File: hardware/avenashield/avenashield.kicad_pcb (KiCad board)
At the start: 4 copper layers, 115 x 78 mm, 128 parts, among them J1 Bus_PCI_Express_Mini, J10 Lattepanda Lower Left Header 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, J11 12V DC IN Headers, J12 EXT PWR IN, J13 LED_OUT, J14 JAE_MM60-EZH059-B5-R650, J2 SIM_Card, J3 CAN_TRA_HEADER, J4 CAN_IMP_HEADER, J5 USB Headers Board Top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

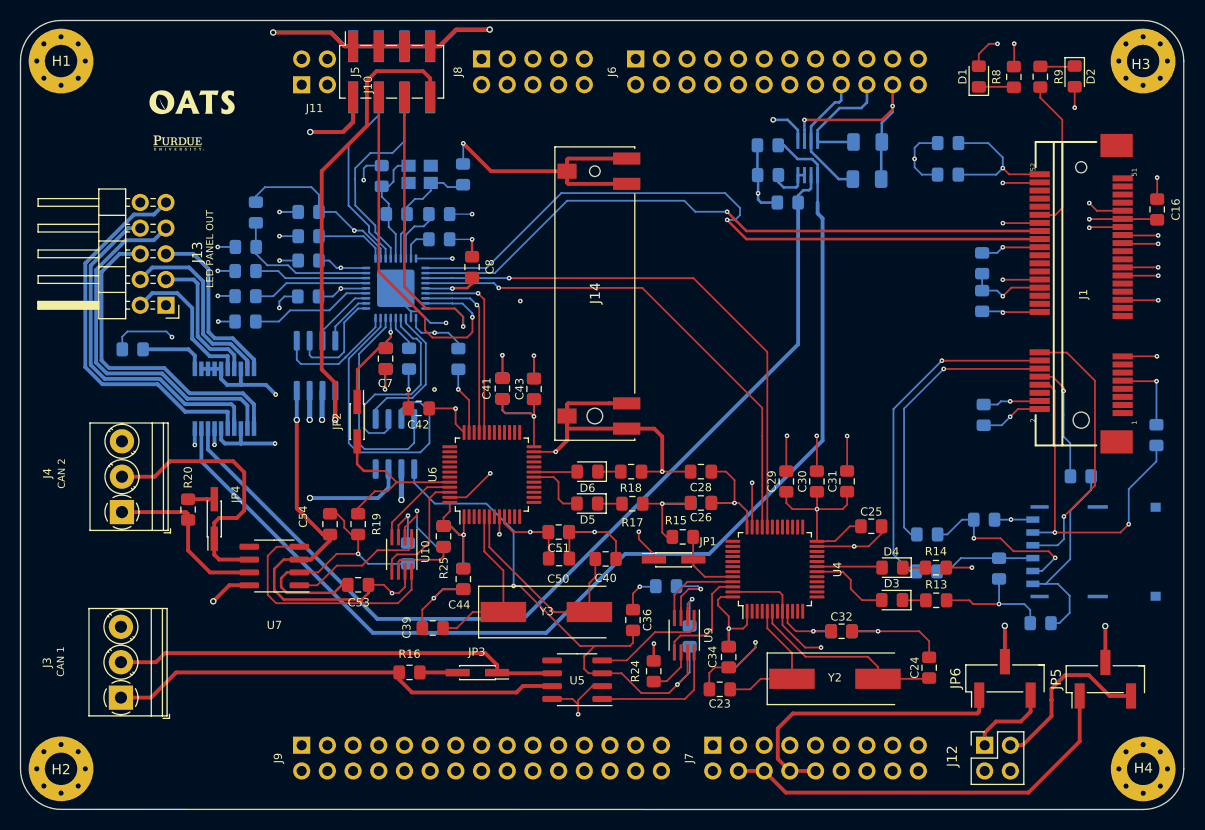
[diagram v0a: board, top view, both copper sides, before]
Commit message: Improved I2C bus routing
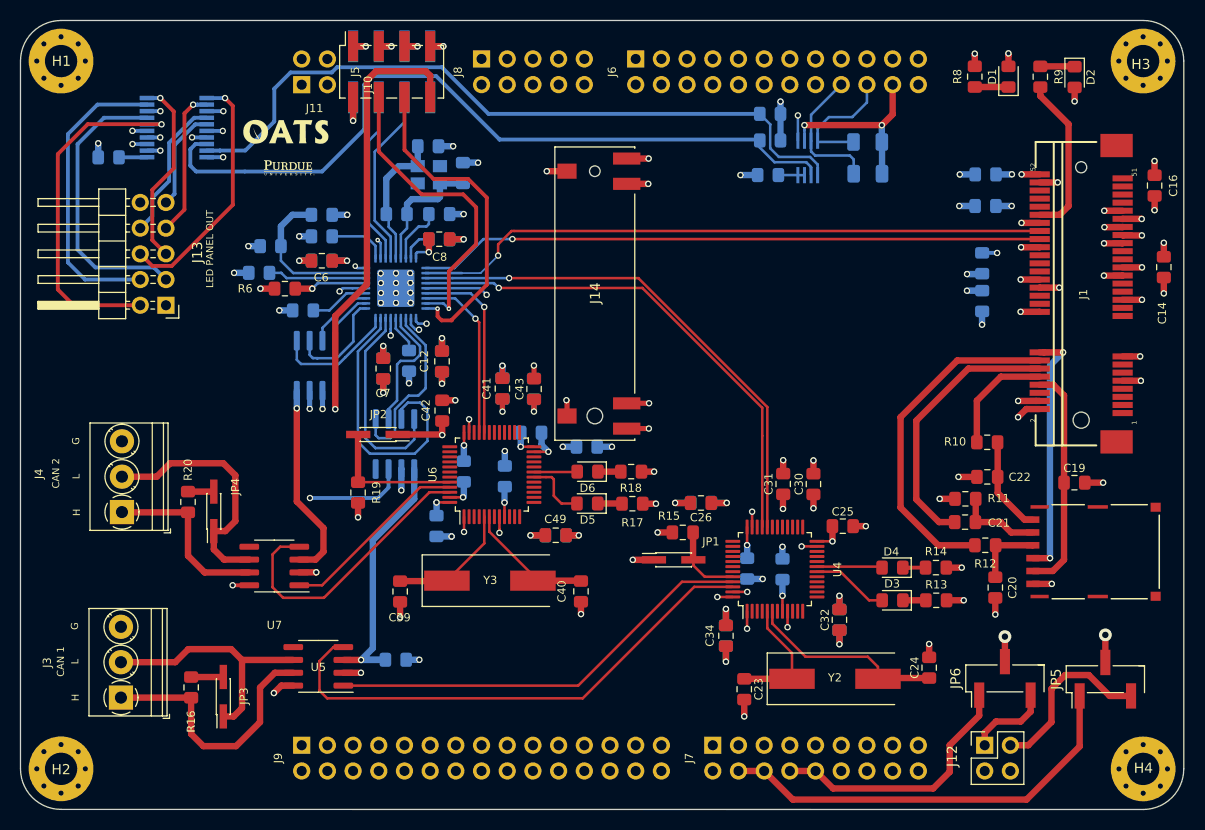
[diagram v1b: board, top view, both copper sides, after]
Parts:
- removed C37, C38, C53, C54: 0.1u, Capacitor_SMD:C_0805_2012Metric_Pad1.15x1.40mm_HandSolder
- removed R24, R25: 10k, Resistor_SMD:R_0805_2012Metric_Pad1.15x1.40mm_HandSolder
- removed U10, U9: TXS0102DCT, Package_SO:SSOP-8_2.95x2.8mm_P0.65mm
- C12, C14, C19, C20, C21, C22, C49, C6, J2, R10, R11, R12, R6: moved to F.Cu
- C28, C29, C36, C44, C50, C51: moved to B.Cu
- moved U8 27.2 mm to (67.1, 89.2), turned to 0 degrees
- moved U5 25.6 mm to (81.1, 142.5)
- moved JP3 25.2 mm to (71.7, 145.5), turned to 90 degrees
- moved C36 23.8 mm to (88.8, 141.8), turned to 180 degrees
- moved C14 23.0 mm to (164.7, 103.0), turned to 270 degrees
- moved R16 21.6 mm to (68.5, 144.6), turned to 90 degrees
- moved R23 19.1 mm to (60.4, 92.2)
- moved C47 17.9 mm to (107.7, 120.8), turned to 0 degrees
- moved C44 15.9 mm to (102.2, 119.4), turned to 0 degrees
- moved C22 15.4 mm to (147.3, 123.8)
- moved C12 14.7 mm to (93.3, 112.3), turned to 270 degrees
- moved G*** 11.2 mm to (78.2, 93.2)
- moved C28 10.6 mm to (123.5, 132.8), turned to 270 degrees
- moved R10 9.84 mm to (147.2, 120.3)
- moved C50 9.74 mm to (99.6, 123.7), turned to 90 degrees
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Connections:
- net /Lattepanda/BOARD_1V8 renamed /Lattepanda/PANDA_1V8
- net /Lattepanda/BOARD_SCL renamed /Lattepanda/PANDA_SCL
- net /Lattepanda/BOARD_SDA renamed /Lattepanda/PANDA_SDA
- net /USB2CAN_IMP/BOARD_5V renamed /USB_HUB/PRT_PWR_3
- net /USB2CAN_TRA/BOARD_5V renamed /USB_HUB/PRT_PWR_2
- net /USB_HEADERS/BOARD_5V renamed /USB_HUB/PRT_PWR_4
- net Net-(J7-Pad10) renamed /Lattepanda/PANDA_5V
- net Net-(J7-Pad4) renamed /Lattepanda/PANDA_3V3
- U4 pad 45: Net-(U4-Pad45) -> /USB2CAN_TRA/CAN_RX
- U4 pad 46: Net-(U4-Pad46) -> /USB2CAN_TRA/CAN_TX
- U5 pad 1: Net-(U5-Pad1) -> /USB2CAN_TRA/CAN_RX
- U5 pad 4: Net-(U5-Pad4) -> /USB2CAN_TRA/CAN_TX
- U6 pad 45: Net-(U10-Pad4) -> /USB2CAN_IMP/CAN_RX
- U6 pad 46: Net-(U10-Pad5) -> /USB2CAN_IMP/CAN_TX
- U7 pad 1: Net-(U10-Pad1) -> /USB2CAN_IMP/CAN_RX
- U7 pad 4: Net-(U10-Pad8) -> /USB2CAN_IMP/CAN_TX
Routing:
- net GNDREF: track 460.1 -> 183.2 mm, vias 71 -> 112
- net +3V3: track 215.7 -> 104.9 mm, vias 26 -> 46
- net /USB2CAN_TRA/CAN_TX: track 0.00 -> 51.6 mm
- net /USB2CAN_TRA/CAN_RX: track 0.00 -> 42.8 mm
- net Net-(R22-Pad2): track 111.7 -> 72.1 mm
- net /USB2CAN_IMP/CAN_TX: track 0.00 -> 28.5 mm
- net Net-(J13-Pad9): track 38.3 -> 10.1 mm
- net /USB_HUB/PRT_PWR_2: track 55.3 -> 27.5 mm, vias 2 -> 1
- net Net-(U10-Pad8): track 24.3 -> 0.00 mm
- net Net-(J13-Pad7): track 36.8 -> 14.7 mm, vias 0 -> 1
- net /USB_HUB/PRT_PWR_3: track 41.8 -> 19.7 mm, vias 2 -> 1
- net Net-(J13-Pad2): track 14.7 -> 35.1 mm, vias 0 -> 1
- net Net-(J13-Pad8): track 34.3 -> 14.4 mm
- net Net-(R21-Pad2): track 96.2 -> 76.5 mm
- net /USB2CAN_TRA/CAN_L: track 44.3 -> 25.0 mm
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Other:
- rule trace_min: 0.088 -> 0.09
- rule via_min_size: 0.4572 -> 0.45
- board text added: "G"
- board text added: "H"
- board text added: "L"
